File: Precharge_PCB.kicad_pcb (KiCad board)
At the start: 2 copper layers, 180 x 100.4 mm, 172 parts, among them J1 Conn_01x02, J2 Conn_01x02, J3 Conn_01x02, J4 Conn_01x02, J5 Conn_01x08, J6 Conn_01x03, J7 Conn_01x04, J8 Conn_01x04, J9 Conn_01x06, K1 G2RL-1A, K2 G2RL-1A, K3 G9EJH-1-E, K4 SPU01L-05, Q1 DMN61D8LQ, Q2 DMN61D8LQ, Q3 DMN61D8LQ, Q4 DMN61D8LQ, Q5 DMN61D8LQ, Q6 DMN61D8LQ, Q7 DMN61D8LQ, Q8 DMN61D8LQ, SW1 SW_Push, U1 TPS7B88, U2 MCP1700x-330xxMB, U3 STM32F103C8Tx, U4 SN65HVD1050D, U5 LM393, U6 4N35, U7 AMC1351, U8 AMC1351, U9 TLV6002, Y1 8M

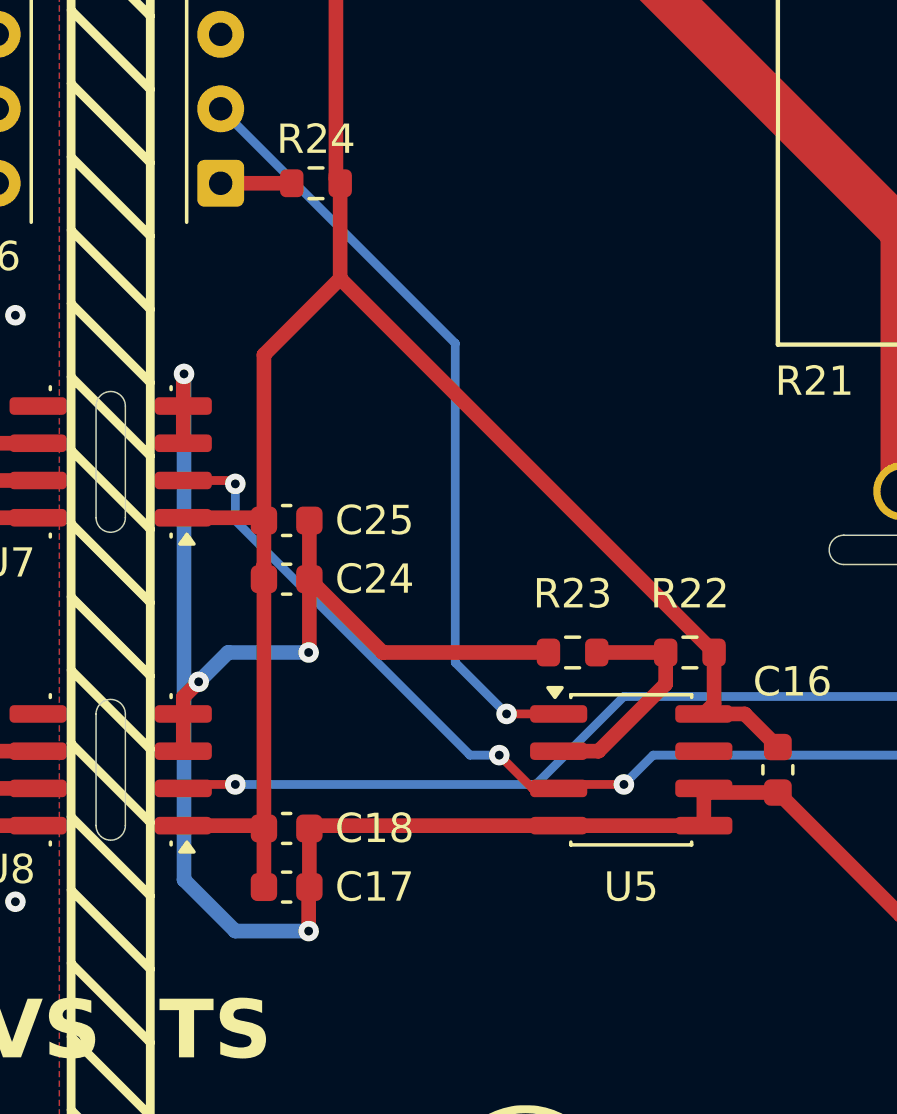
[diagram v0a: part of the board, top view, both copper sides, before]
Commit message: *: Add filter capacitors on HV sense inputs
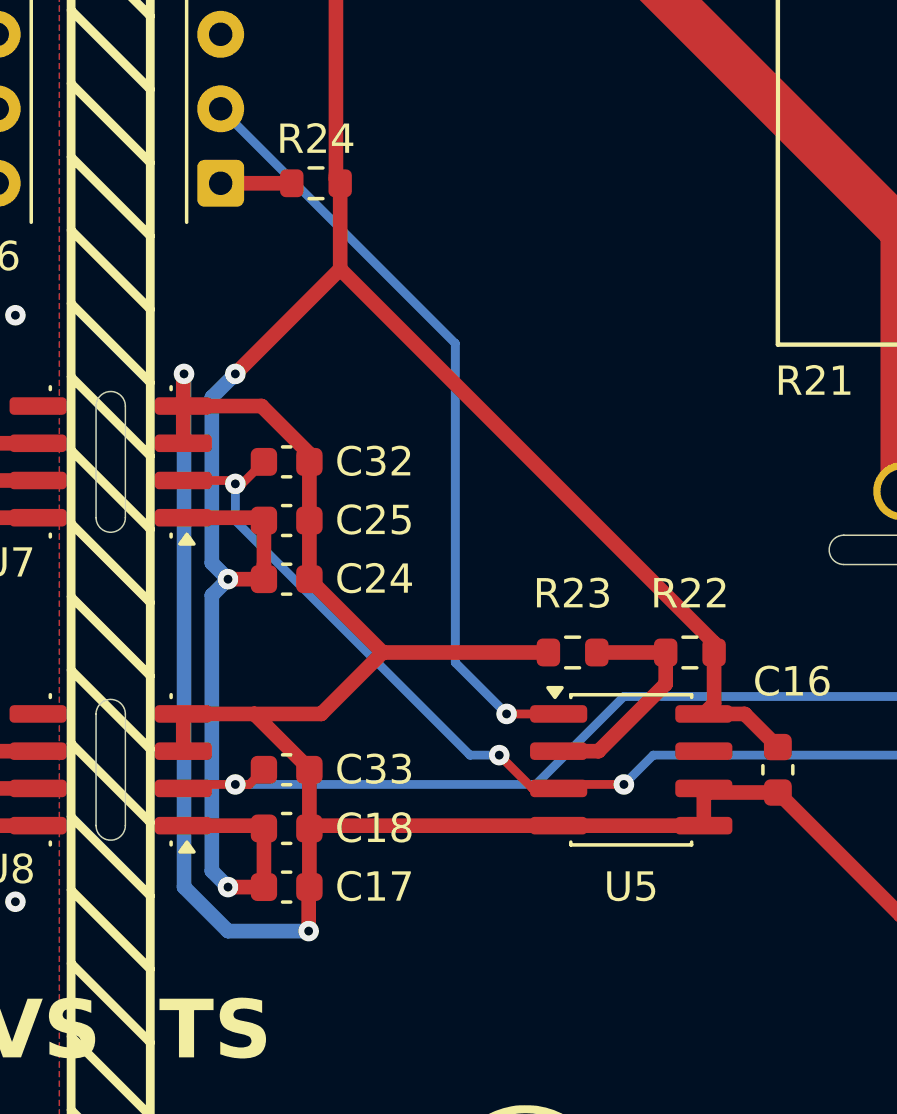
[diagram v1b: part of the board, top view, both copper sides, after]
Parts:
- added C32: 1n, Capacitor_SMD:C_0603_1608Metric, F.Cu at (186.8, 100.0)
- added C33: 1n, Capacitor_SMD:C_0603_1608Metric, F.Cu at (186.8, 110.5)
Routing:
- net GND1: track 253.2 -> 265.0 mm, vias 4 -> 2
- net +5VA: track 74.2 -> 81.9 mm, vias 0 -> 3
- net /HV Sampling/ACC Sampler/SCALED: track 47.8 -> 49.1 mm
- net /HV Sampling/TS Sampler/SCALED: track 53.3 -> 54.4 mm

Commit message: *: Change single-ended conversion bias resistors from 10k to 1k
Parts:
- R38, R39, R51, R52: value 10k -> 1k
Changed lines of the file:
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@@
 			)
 		)
-		(property "Value" "10k"
+		(property "Value" "1k"
 			(at 0 1.43 0)
 			(layer "F.Fab")
@@
 			)
 		)
-		(property "Dist #" "C25804"
+		(property "Dist #" "C21190"
 			(at 0 0 0)
 			(unlocked yes)
@@
 			)
 		)
-		(property "Mfr #" "0603WAF1002T5E"
+		(property "Mfr #" "0603WAF1001T5E"
 			(at 0 0 0)
 			(unlocked yes)
@@
 			)
 		)
-		(property "Value" "10k"
+		(property "Value" "1k"
 			(at 0 1.43 0)
 			(layer "F.Fab")
@@
 			)
 		)
-		(property "Dist #" "C25804"
+		(property "Dist #" "C21190"
 			(at 0 0 180)
 			(unlocked yes)
@@
 			)
 		)
-		(property "Mfr #" "0603WAF1002T5E"
+		(property "Mfr #" "0603WAF1001T5E"
 			(at 0 0 180)
 			(unlocked yes)
@@
 			)
 		)
-		(property "Value" "10k"
+		(property "Value" "1k"
 			(at 0 1.43 0)
 			(layer "F.Fab")
@@
 			)
 		)
-		(property "Dist #" "C25804"
+		(property "Dist #" "C21190"
 			(at 0 0 180)
 			(unlocked yes)
@@
 			)
 		)
-		(property "Mfr #" "0603WAF1002T5E"
+		(property "Mfr #" "0603WAF1001T5E"
 			(at 0 0 180)
 			(unlocked yes)
@@
 			)
 		)
-		(property "Value" "10k"
+		(property "Value" "1k"
 			(at 0 1.43 0)
 			(layer "F.Fab")
@@
 			)
 		)
-		(property "Dist #" "C25804"
+		(property "Dist #" "C21190"
 			(at 0 0 0)
 			(unlocked yes)
@@
 			)
 		)
-		(property "Mfr #" "0603WAF1002T5E"
+		(property "Mfr #" "0603WAF1001T5E"
 			(at 0 0 0)
 			(unlocked yes)

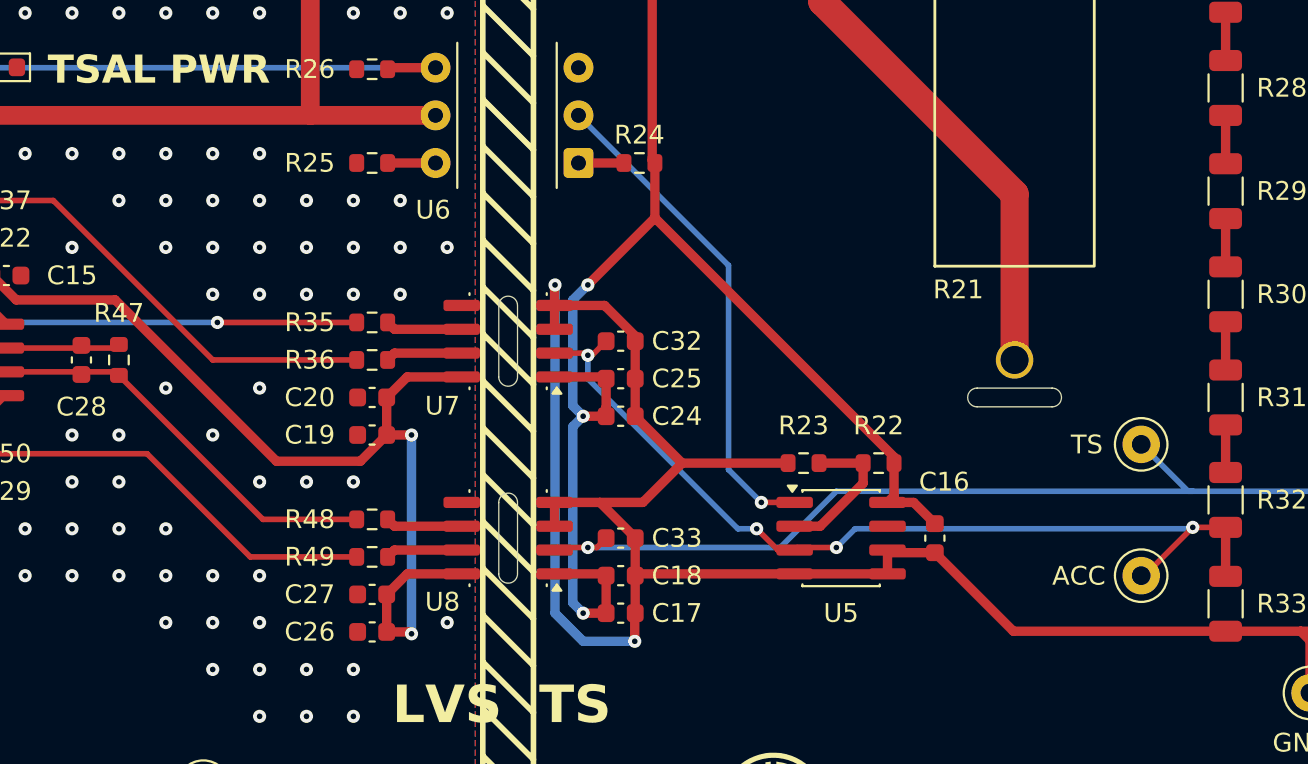
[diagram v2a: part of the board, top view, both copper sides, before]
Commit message: *: Fix AMC1351 footprint
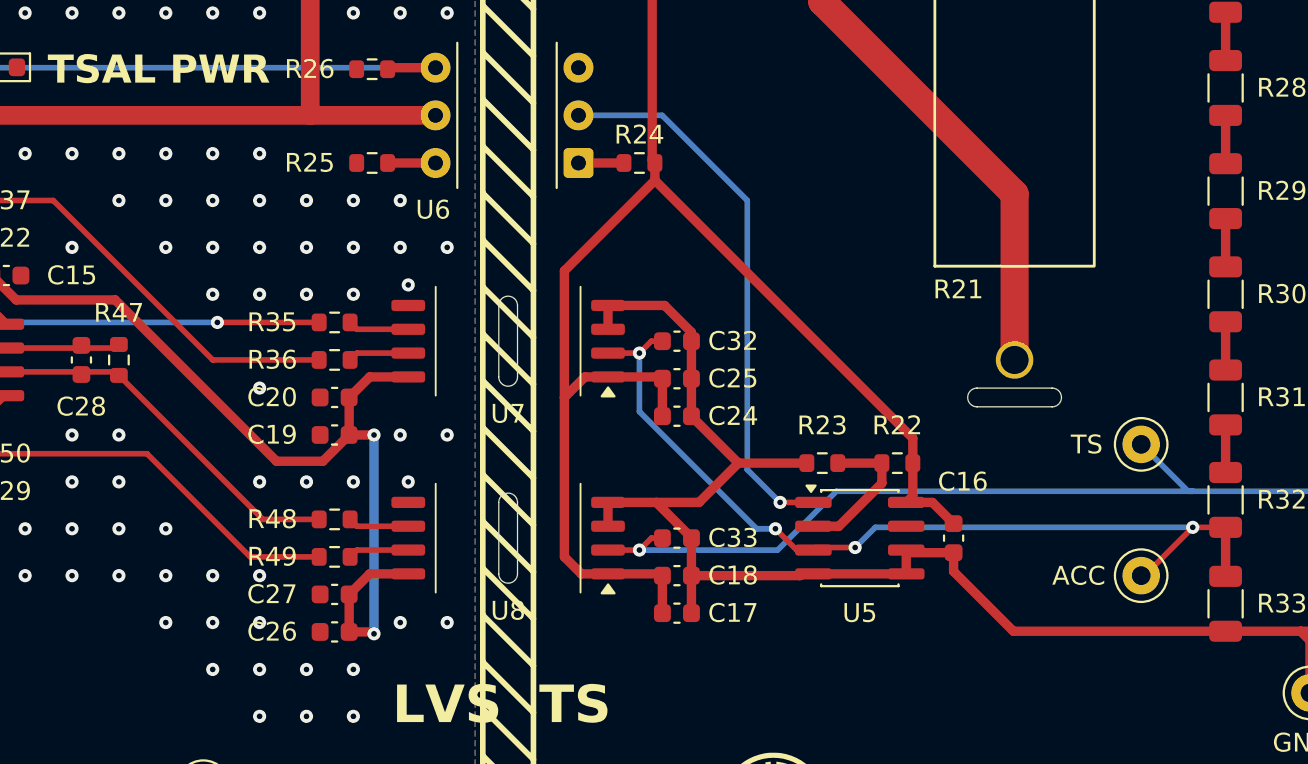
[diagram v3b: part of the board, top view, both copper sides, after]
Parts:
- U7, U8: footprint Package_SO:SOIC-8_3.9x4.9mm_P1.27mm -> Package_SO:SOIC-8_7.5x5.85mm_P1.27mm
- moved C17 3.00 mm to (189.8, 114.5)
- moved C18 3.00 mm to (189.8, 112.5)
- moved C24 3.00 mm to (189.8, 104.0)
- moved C25 3.00 mm to (189.8, 102.0)
- moved C32 3.00 mm to (189.8, 100.0)
- moved C33 3.00 mm to (189.8, 110.5)
- moved C19 2.00 mm to (171.5, 105.0)
- moved C20 2.00 mm to (171.5, 103.0)
- moved C26 2.00 mm to (171.5, 115.5)
- moved C27 2.00 mm to (171.5, 113.5)
- moved R35 2.00 mm to (171.5, 99.0)
- moved R36 2.00 mm to (171.5, 101.0)
- moved R48 2.00 mm to (171.5, 109.5)
- moved R49 2.00 mm to (171.5, 111.5)
- moved C16 1.00 mm to (204.5, 110.5)
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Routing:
- net GND1: track 265.0 -> 236.2 mm, vias 2 -> 0
- net +3V3: track 201.7 -> 198.0 mm
- net Net-(U5-Pad1): track 26.4 -> 29.5 mm
- net /HV Sampling/TS Sampler/SCALED: track 54.4 -> 51.9 mm
- net +5VA: track 81.9 -> 84.1 mm, vias 3 -> 0
- net Net-(U9B--): track 22.0 -> 20.0 mm
- net Net-(U9B-+): track 29.8 -> 27.8 mm
- net Net-(U9A--): track 29.8 -> 27.8 mm
- net Net-(U9A-+): track 35.9 -> 33.9 mm
- net /HV Sampling/ACC Sampler/SCALED: track 49.1 -> 47.6 mm
- net Net-(U8-OUTP): track 4.10 -> 3.25 mm
- net Net-(U8-OUTN): track 4.10 -> 3.25 mm
- net Net-(U7-OUTP): track 4.10 -> 3.25 mm
- net Net-(U7-OUTN): track 4.10 -> 3.25 mm
- net GND: vias 353 -> 355

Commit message: *: Set precharge comparator threshold resistors and add capacitor
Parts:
- added C34: 1u, Capacitor_SMD:C_0603_1608Metric, F.Cu at (197.5, 104.5)
- R22: value R -> 18k
- R23: value R -> 1k2
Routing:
- net Net-(U5A--): track 8.02 -> 10.0 mm
- net GND1: track 236.2 -> 238.2 mm

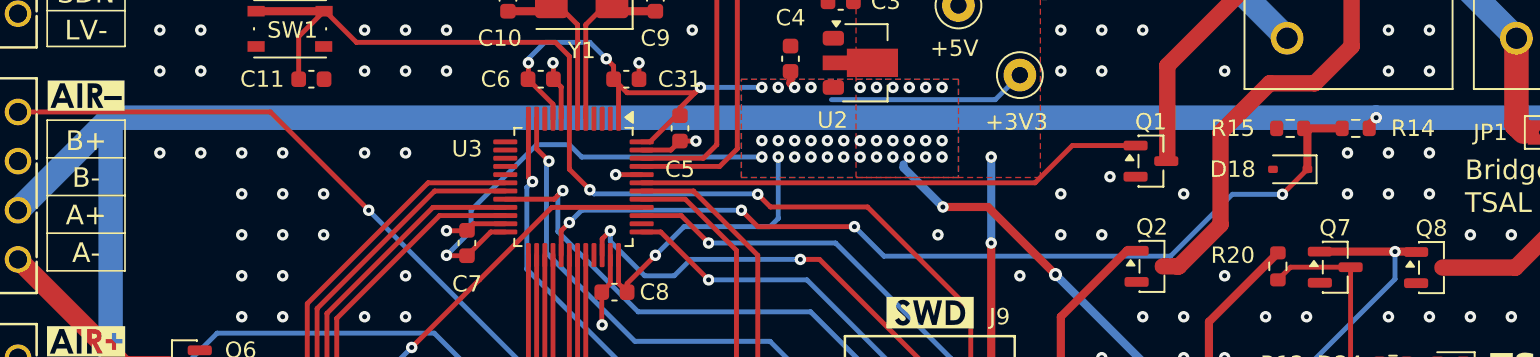
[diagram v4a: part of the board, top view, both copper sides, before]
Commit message: *: Measure shutdown voltage with STM ADC
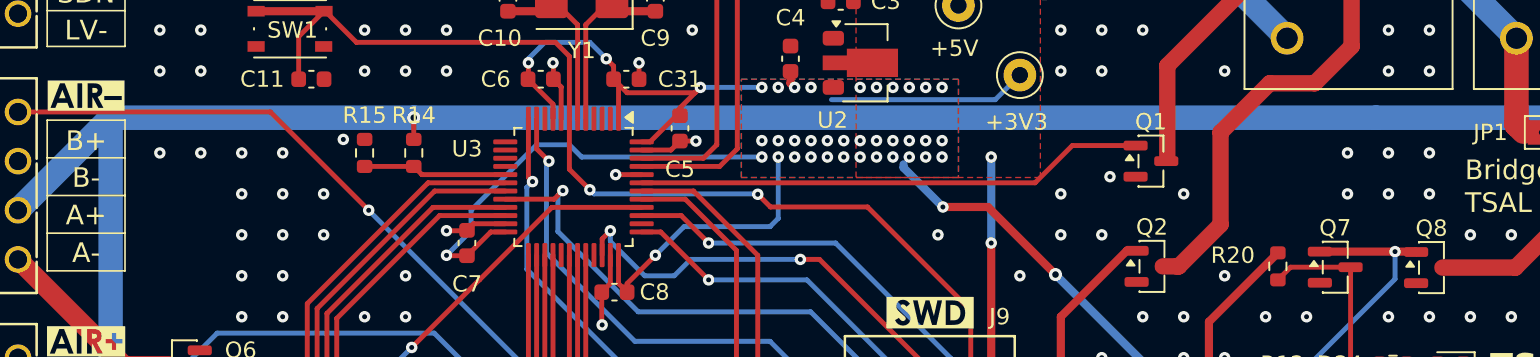
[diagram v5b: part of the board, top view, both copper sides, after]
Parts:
- removed D18: 3V6, Diode_SMD:D_SOD-323
- moved R14 57.5 mm to (90.5, 72.5), turned to -90 degrees
- moved R15 56.5 mm to (87.5, 72.5), turned to 90 degrees
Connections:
- U3 pad 17: unconnected-(U3-PA7-Pad17) -> SHUTDOWN_3V3
- U3 pad 29: SHUTDOWN_3V3 -> unconnected-(U3-PA8-Pad29)
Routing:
- net SHUTDOWN_3V3: track 55.9 -> 8.79 mm, vias 4 -> 0
- net GND: vias 355 -> 354

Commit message: bom: Switch from 1N4007 to BYG20J
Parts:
- D16, D17, D21, D23: value 1N4007 -> BYG20J
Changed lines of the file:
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@@
 			)
 		)
-		(property "Value" "1N4007"
+		(property "Value" "BYG20J"
 			(at -0.000001 2.600002 0)
 			(layer "F.Fab")
@@
 			)
 		)
-		(property "Dist #" "C20754788"
+		(property "Dist #" "C241925"
 			(at 0 0 0)
 			(unlocked yes)
@@
 			)
 		)
-		(property "Mfr" "JSMSEMI"
+		(property "Mfr" "VISHAY"
 			(at 0 0 0)
 			(unlocked yes)
@@
 			)
 		)
-		(property "Mfr #" "1N4007 M7"
+		(property "Mfr #" "BYG20J-E3/TR"
 			(at 0 0 0)
 			(unlocked yes)
@@
 			)
 		)
-		(property "Value" "1N4007"
+		(property "Value" "BYG20J"
 			(at 0 2.600001 90)
 			(layer "F.Fab")
@@
 			)
 		)
-		(property "Datasheet" "http://www.vishay.com/docs/88503/1n4001.pdf"
+		(property "Datasheet" ""
 			(at 0 0 90)
 			(unlocked yes)
@@
 			)
 		)
-		(property "Description" "1000V 1A General Purpose Rectifier Diode, DO-41"
+		(property "Description" ""
 			(at 0 0 90)
 			(unlocked yes)
@@
 			)
 		)
-		(property "Dist #" "C20754788"
+		(property "Dist #" "C241925"
 			(at 0 0 90)
 			(unlocked yes)
@@
 			)
 		)
-		(property "Mfr" "JSMSEMI"
+		(property "Mfr" "VISHAY"
 			(at 0 0 90)
 			(unlocked yes)
@@
 			)
 		)
-		(property "Mfr #" "1N4007 M7"
+		(property "Mfr #" "BYG20J-E3/TR"
 			(at 0 0 90)
 			(unlocked yes)
@@
 			)
 		)
-		(property "Value" "1N4007"
+		(property "Value" "BYG20J"
 			(at -0.000001 2.600002 0)
 			(layer "F.Fab")
@@
 			)
 		)
-		(property "Dist #" "C20754788"
+		(property "Dist #" "C241925"
 			(at 0 0 0)
 			(unlocked yes)
@@
 			)
 		)
-		(property "Mfr" "JSMSEMI"
+		(property "Mfr" "VISHAY"
 			(at 0 0 0)
 			(unlocked yes)
@@
 			)
 		)
-		(property "Mfr #" "1N4007 M7"
+		(property "Mfr #" "BYG20J-E3/TR"
 			(at 0 0 0)
 			(unlocked yes)
@@
 			)
 		)
-		(property "Value" "1N4007"
+		(property "Value" "BYG20J"
 			(at 0 2.600001 0)
 			(layer "F.Fab")
@@
 			)
 		)
-		(property "Dist #" "C20754788"
+		(property "Dist #" "C241925"
 			(at 0 0 0)
 			(unlocked yes)
@@
 			)
 		)
-		(property "Mfr" "JSMSEMI"
+		(property "Mfr" "VISHAY"
 			(at 0 0 0)
 			(unlocked yes)
@@
 			)
 		)
-		(property "Mfr #" "1N4007 M7"
+		(property "Mfr #" "BYG20J-E3/TR"
 			(at 0 0 0)
 			(unlocked yes)
